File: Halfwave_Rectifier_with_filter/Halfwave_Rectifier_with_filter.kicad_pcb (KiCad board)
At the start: 4 copper layers, 25.5 x 19 mm, 10 parts, among them J1 Screw_Terminal_01x02, J2 Conn_01x02_Pin, T1 Transformer_1P_1S

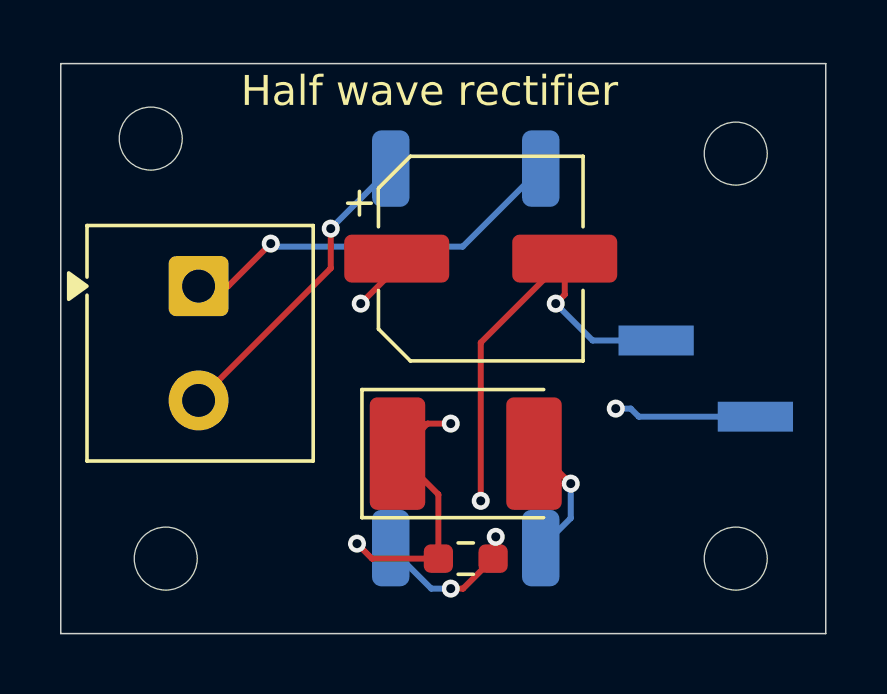
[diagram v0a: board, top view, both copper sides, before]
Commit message: Through holes changes to buried
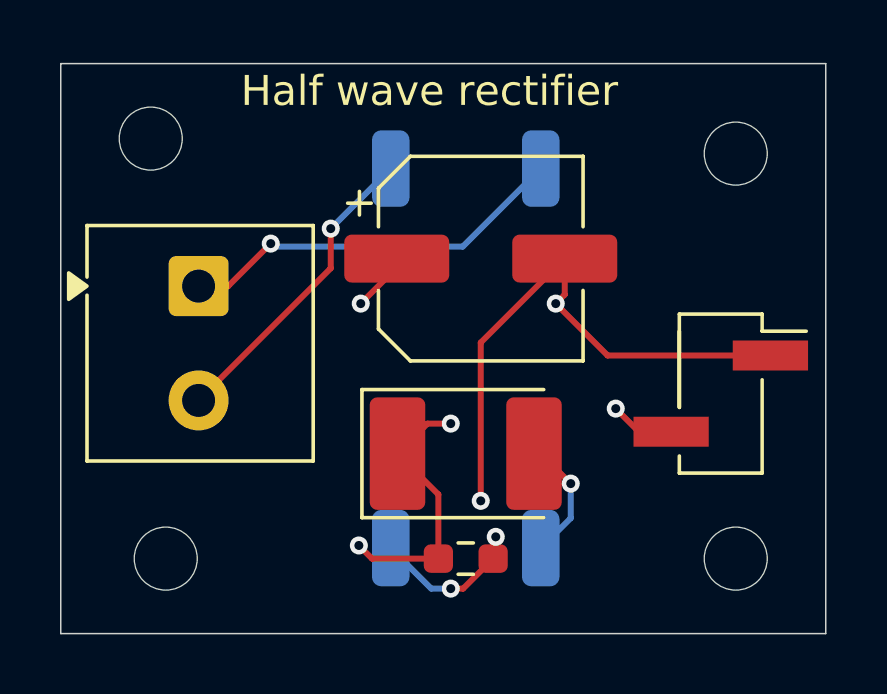
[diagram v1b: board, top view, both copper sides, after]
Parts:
- J2: moved to F.Cu
- moved J2 0.71 mm to (148.0, 74.0), turned to 0 degrees
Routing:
- net GND: track 21.3 -> 25.3 mm
- net Net-(D1-K): track 29.8 -> 27.2 mm
